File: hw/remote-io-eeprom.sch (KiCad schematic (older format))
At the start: 7 parts, among them P2 CONN_01X02, U3 CAT24C32

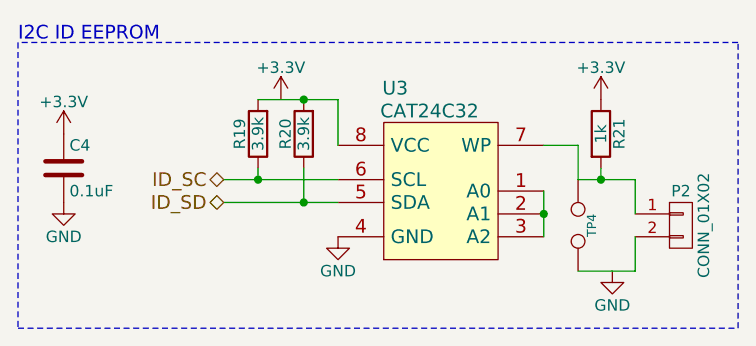
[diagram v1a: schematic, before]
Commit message: Matched all footprints to schem and created kicad_pcb file
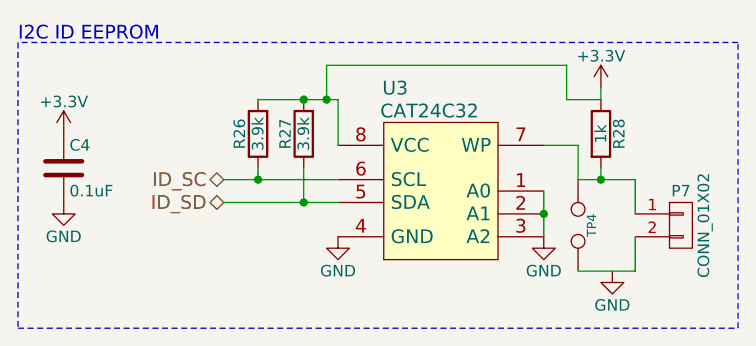
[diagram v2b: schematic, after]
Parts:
- C4: footprint (none) -> Capacitors_SMD:C_0805_HandSoldering
- P7: renamed from P2; footprint (none) -> Pin_Headers:Pin_Header_Straight_1x02
- R26: renamed from R19; footprint (none) -> Resistors_SMD:R_0805_HandSoldering
- R27: renamed from R20; footprint (none) -> Resistors_SMD:R_0805_HandSoldering
- R28: renamed from R21; footprint (none) -> Resistors_SMD:R_0805_HandSoldering
- TP4: footprint (none) -> Connect:TESTPOINT
- U3: footprint (none) -> Housings_SOIC:SOIC-8_3.9x4.9mm_Pitch1.27mm
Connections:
- net +3V3: now also R26.2, R27.2, U3.8 (VCC)
- net GND: now also U3.1 (A0), U3.2 (A1), U3.3 (A2)
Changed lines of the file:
@@
 F 0 "U3" H 4850 3500 60  0000 C CNN
 F 1 "CAT24C32" H 5000 3400 60  0000 C CNN
-F 2 "" H 5200 3050 60  0000 C CNN
+F 2 "Housings_SOIC:SOIC-8_3.9x4.9mm_Pitch1.27mm" H 5200 3050 60  0001 C CNN
 F 3 "" H 5200 3050 60  0000 C CNN
 	1    5050 3100
@@
 F 0 "C4" H 3425 3150 50  0000 L CNN
 F 1 "0.1uF" H 3425 2950 50  0000 L CNN
-F 2 "" H 3438 2900 30  0000 C CNN
+F 2 "Capacitors_SMD:C_0805_HandSoldering" H 3438 2900 30  0001 C CNN
 F 3 "" H 3400 3050 60  0000 C CNN
 	1    3400 3050
@@
 F 0 "TP4" H 5650 3360 40  0000 C CNN
 F 1 "TEST" H 5650 3230 40  0001 C CNN
-F 2 "" H 5650 3300 60  0000 C CNN
+F 2 "Connect:TESTPOINT" H 5650 3300 60  0001 C CNN
 F 3 "" H 5650 3300 60  0000 C CNN
 	1    5650 3300
@@
 $EndComp
 $Comp
-L CONN_01X02 P2
+L CONN_01X02 P7
 U 1 1 558185B6
 P 6100 3300
-F 0 "P2" H 6100 3450 50  0000 C CNN
+F 0 "P7" H 6100 3450 50  0000 C CNN
 F 1 "CONN_01X02" V 6200 3300 50  0000 C CNN
-F 2 "" H 6100 3300 60  0000 C CNN
+F 2 "Pin_Headers:Pin_Header_Straight_1x02" H 6100 3300 60  0001 C CNN
 F 3 "" H 6100 3300 60  0000 C CNN
 	1    6100 3300
@@
 $EndComp
 $Comp
-L R R21
+L R R28
 U 1 1 55818601
 P 5750 2900
-F 0 "R21" V 5830 2900 50  0000 C CNN
+F 0 "R28" V 5830 2900 50  0000 C CNN
 F 1 "1k" V 5750 2900 50  0000 C CNN
-F 2 "" V 5680 2900 30  0000 C CNN
+F 2 "Resistors_SMD:R_0805_HandSoldering" V 5680 2900 30  0001 C CNN
 F 3 "" H 5750 2900 30  0000 C CNN
 	1    5750 2900
@@
 $EndComp
 $Comp
-L R R19
+L R R26
 U 1 1 5581863F
 P 4250 2900
-F 0 "R19" V 4330 2900 50  0000 C CNN
+F 0 "R26" V 4330 2900 50  0000 C CNN
 F 1 "3.9k" V 4250 2900 50  0000 C CNN
-F 2 "" V 4180 2900 30  0000 C CNN
+F 2 "Resistors_SMD:R_0805_HandSoldering" V 4180 2900 30  0001 C CNN
 F 3 "" H 4250 2900 30  0000 C CNN
 	1    4250 2900
@@
 $EndComp
 $Comp
-L R R20
+L R R27
 U 1 1 55818663
 P 4450 2900
-F 0 "R20" V 4530 2900 50  0000 C CNN
+F 0 "R27" V 4530 2900 50  0000 C CNN
 F 1 "3.9k" V 4450 2900 50  0000 C CNN
-F 2 "" V 4380 2900 30  0000 C CNN
+F 2 "Resistors_SMD:R_0805_HandSoldering" V 4380 2900 30  0001 C CNN
 F 3 "" H 4450 2900 30  0000 C CNN
 	1    4450 2900
@@
 $EndComp
 $Comp
-L +3.3V #PWR34
-U 1 1 558186FF
-P 4350 2750
-F 0 "#PWR34" H 4350 2600 50  0001 C CNN
-F 1 "+3.3V" H 4350 2890 50  0000 C CNN
-F 2 "" H 4350 2750 60  0000 C CNN
-F 3 "" H 4350 2750 60  0000 C CNN
-	1    4350 2750
-	1    0    0    -1
-$EndComp
-$Comp
-L +3.3V #PWR36
+L +3.3V #PWR045
 U 1 1 55818752
 P 3400 2900
-F 0 "#PWR36" H 3400 2750 50  0001 C CNN
+F 0 "#PWR045" H 3400 2750 50  0001 C CNN
 F 1 "+3.3V" H 3400 3040 50  0000 C CNN
 F 2 "" H 3400 2900 60  0000 C CNN
@@
 $EndComp
 $Comp
-L GND #PWR37
-U 1 1 55818774
-P 3400 3200
-F 0 "#PWR37" H 3400 2950 50  0001 C CNN
-F 1 "GND" H 3400 3050 50  0000 C CNN
-F 2 "" H 3400 3200 60  0000 C CNN
-F 3 "" H 3400 3200 60  0000 C CNN
-	1    3400 3200
-	1    0    0    -1
-$EndComp
-$Comp
-L GND #PWR38
-U 1 1 55818794
-P 4600 3350
-F 0 "#PWR38" H 4600 3100 50  0001 C CNN
-F 1 "GND" H 4600 3200 50  0000 C CNN
-F 2 "" H 4600 3350 60  0000 C CNN
-F 3 "" H 4600 3350 60  0000 C CNN
-	1    4600 3350
-	1    0    0    -1
-$EndComp
-$Comp
-L GND #PWR39
-U 1 1 55818DF1
-P 5800 3500
-F 0 "#PWR39" H 5800 3250 50  0001 C CNN
-F 1 "GND" H 5800 3350 50  0000 C CNN
-F 2 "" H 5800 3500 60  0000 C CNN
-F 3 "" H 5800 3500 60  0000 C CNN
-	1    5800 3500
-	1    0    0    -1
-$EndComp
-$Comp
-L +3.3V #PWR35
+L +3.3V #PWR046
 U 1 1 558190BD
-P 5750 2750
-F 0 "#PWR35" H 5750 2600 50  0001 C CNN
-F 1 "+3.3V" H 5750 2890 50  0000 C CNN
-F 2 "" H 5750 2750 60  0000 C CNN
-F 3 "" H 5750 2750 60  0000 C CNN
-	1    5750 2750
+P 5750 2700
+F 0 "#PWR046" H 5750 2550 50  0001 C CNN
+F 1 "+3.3V" H 5750 2840 50  0000 C CNN
+F 2 "" H 5750 2700 60  0000 C CNN
+F 3 "" H 5750 2700 60  0000 C CNN
+	1    5750 2700
 	1    0    0    -1
 $EndComp
@@
 Wire Wire Line
 	4250 2750 4600 2750
-Wire Wire Line
-	4600 2750 4600 2950
 Connection ~ 4450 2750
 Wire Wire Line
@@
 Text Notes 3200 2500 0    60   ~ 0
 I2C ID EEPROM
+Wire Wire Line
+	4600 2750 4600 2950
+Wire Wire Line
+	4550 2750 4550 2600
+Wire Wire Line
+	4550 2600 5600 2600
+Wire Wire Line
+	5600 2600 5600 2750
+Wire Wire Line
+	5600 2750 5750 2750
+Connection ~ 4550 2750
+Wire Wire Line
+	5750 2750 5750 2700
+$Comp
+L GND #PWR047
+U 1 1 55818DF1
+P 5800 3500
+F 0 "#PWR047" H 5800 3250 50  0001 C CNN
+F 1 "GND" H 5800 3350 50  0000 C CNN
+F 2 "" H 5800 3500 60  0000 C CNN
+F 3 "" H 5800 3500 60  0000 C CNN
+	1    5800 3500
+	1    0    0    -1
+$EndComp
+$Comp
+L GND #PWR048
+U 1 1 5581AAA1
+P 5500 3350
+F 0 "#PWR048" H 5500 3100 50  0001 C CNN
+F 1 "GND" H 5500 3200 50  0000 C CNN
+F 2 "" H 5500 3350 60  0000 C CNN
+F 3 "" H 5500 3350 60  0000 C CNN
+	1    5500 3350
+	1    0    0    -1
+$EndComp
+$Comp
+L GND #PWR049
+U 1 1 55818794
+P 4600 3350
+F 0 "#PWR049" H 4600 3100 50  0001 C CNN
+F 1 "GND" H 4600 3200 50  0000 C CNN
+F 2 "" H 4600 3350 60  0000 C CNN
+F 3 "" H 4600 3350 60  0000 C CNN
+	1    4600 3350
+	1    0    0    -1
+$EndComp
+$Comp
+L GND #PWR050
+U 1 1 55818774
+P 3400 3200
+F 0 "#PWR050" H 3400 2950 50  0001 C CNN
+F 1 "GND" H 3400 3050 50  0000 C CNN
+F 2 "" H 3400 3200 60  0000 C CNN
+F 3 "" H 3400 3200 60  0000 C CNN
+	1    3400 3200
+	1    0    0    -1
+$EndComp
 $EndSCHEMATC

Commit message: removed autosave
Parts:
- TP4: footprint Connect:TESTPOINT -> Pin_Headers:Pin_Header_Straight_1x02
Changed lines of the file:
@@
 F 0 "TP4" H 5650 3360 40  0000 C CNN
 F 1 "TEST" H 5650 3230 40  0001 C CNN
-F 2 "Connect:TESTPOINT" H 5650 3300 60  0001 C CNN
+F 2 "Pin_Headers:Pin_Header_Straight_1x02" H 5650 3300 60  0001 C CNN
 F 3 "" H 5650 3300 60  0000 C CNN
 	1    5650 3300

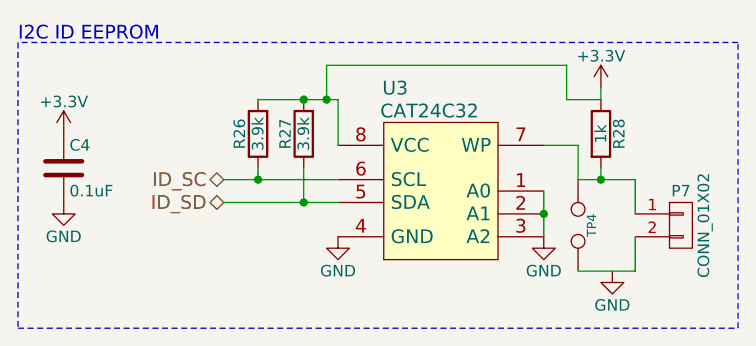
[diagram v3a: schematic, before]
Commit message: added CAN power, controller, and transceiver to schem and updated PCB
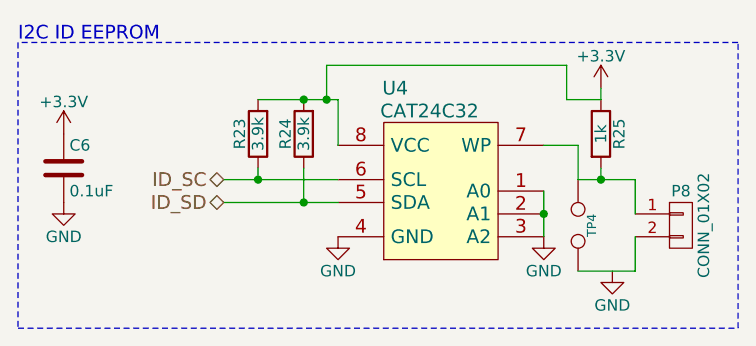
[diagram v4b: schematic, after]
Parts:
- renumbered C4 to C6, P7 to P8, R26 to R23, R27 to R24, R28 to R25, U3 to U4
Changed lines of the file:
@@
 $Descr USLetter 11000 8500
 encoding utf-8
-Sheet 4 5
+Sheet 4 6
 Title "I2C ID EEPROM"
 Date "2015-06-15"
@@
 $EndDescr
 $Comp
-L CAT24C32 U3
+L CAT24C32 U4
 U 1 1 558183DB
 P 5050 3100
-F 0 "U3" H 4850 3500 60  0000 C CNN
+F 0 "U4" H 4850 3500 60  0000 C CNN
 F 1 "CAT24C32" H 5000 3400 60  0000 C CNN
 F 2 "Housings_SOIC:SOIC-8_3.9x4.9mm_Pitch1.27mm" H 5200 3050 60  0001 C CNN
@@
 $EndComp
 $Comp
-L C C4
+L C C6
 U 1 1 5581842A
 P 3400 3050
-F 0 "C4" H 3425 3150 50  0000 L CNN
+F 0 "C6" H 3425 3150 50  0000 L CNN
 F 1 "0.1uF" H 3425 2950 50  0000 L CNN
 F 2 "Capacitors_SMD:C_0805_HandSoldering" H 3438 2900 30  0001 C CNN
@@
 $EndComp
 $Comp
-L CONN_01X02 P7
+L CONN_01X02 P8
 U 1 1 558185B6
 P 6100 3300
-F 0 "P7" H 6100 3450 50  0000 C CNN
+F 0 "P8" H 6100 3450 50  0000 C CNN
 F 1 "CONN_01X02" V 6200 3300 50  0000 C CNN
 F 2 "Pin_Headers:Pin_Header_Straight_1x02" H 6100 3300 60  0001 C CNN
@@
 $EndComp
 $Comp
-L R R28
+L R R25
 U 1 1 55818601
 P 5750 2900
-F 0 "R28" V 5830 2900 50  0000 C CNN
+F 0 "R25" V 5830 2900 50  0000 C CNN
 F 1 "1k" V 5750 2900 50  0000 C CNN
 F 2 "Resistors_SMD:R_0805_HandSoldering" V 5680 2900 30  0001 C CNN
@@
 $EndComp
 $Comp
-L R R26
+L R R23
 U 1 1 5581863F
 P 4250 2900
-F 0 "R26" V 4330 2900 50  0000 C CNN
+F 0 "R23" V 4330 2900 50  0000 C CNN
 F 1 "3.9k" V 4250 2900 50  0000 C CNN
 F 2 "Resistors_SMD:R_0805_HandSoldering" V 4180 2900 30  0001 C CNN
@@
 $EndComp
 $Comp
-L R R27
+L R R24
 U 1 1 55818663
 P 4450 2900
-F 0 "R27" V 4530 2900 50  0000 C CNN
+F 0 "R24" V 4530 2900 50  0000 C CNN
 F 1 "3.9k" V 4450 2900 50  0000 C CNN
 F 2 "Resistors_SMD:R_0805_HandSoldering" V 4380 2900 30  0001 C CNN
@@
 $EndComp
 $Comp
-L +3.3V #PWR045
+L +3.3V #PWR051
 U 1 1 55818752
 P 3400 2900
-F 0 "#PWR045" H 3400 2750 50  0001 C CNN
+F 0 "#PWR051" H 3400 2750 50  0001 C CNN
 F 1 "+3.3V" H 3400 3040 50  0000 C CNN
 F 2 "" H 3400 2900 60  0000 C CNN
@@
 $EndComp
 $Comp
-L +3.3V #PWR046
+L +3.3V #PWR052
 U 1 1 558190BD
 P 5750 2700
-F 0 "#PWR046" H 5750 2550 50  0001 C CNN
+F 0 "#PWR052" H 5750 2550 50  0001 C CNN
 F 1 "+3.3V" H 5750 2840 50  0000 C CNN
 F 2 "" H 5750 2700 60  0000 C CNN
@@
 	5750 2750 5750 2700
 $Comp
-L GND #PWR047
+L GND #PWR053
 U 1 1 55818DF1
 P 5800 3500
-F 0 "#PWR047" H 5800 3250 50  0001 C CNN
+F 0 "#PWR053" H 5800 3250 50  0001 C CNN
 F 1 "GND" H 5800 3350 50  0000 C CNN
 F 2 "" H 5800 3500 60  0000 C CNN
@@
 $EndComp
 $Comp
-L GND #PWR048
+L GND #PWR054
 U 1 1 5581AAA1
 P 5500 3350
-F 0 "#PWR048" H 5500 3100 50  0001 C CNN
+F 0 "#PWR054" H 5500 3100 50  0001 C CNN
 F 1 "GND" H 5500 3200 50  0000 C CNN
 F 2 "" H 5500 3350 60  0000 C CNN
@@
 $EndComp
 $Comp
-L GND #PWR049
+L GND #PWR055
 U 1 1 55818794
 P 4600 3350
-F 0 "#PWR049" H 4600 3100 50  0001 C CNN
+F 0 "#PWR055" H 4600 3100 50  0001 C CNN
 F 1 "GND" H 4600 3200 50  0000 C CNN
 F 2 "" H 4600 3350 60  0000 C CNN
@@
 $EndComp
 $Comp
-L GND #PWR050
+L GND #PWR056
 U 1 1 55818774
 P 3400 3200
-F 0 "#PWR050" H 3400 2950 50  0001 C CNN
+F 0 "#PWR056" H 3400 2950 50  0001 C CNN
 F 1 "GND" H 3400 3050 50  0000 C CNN
 F 2 "" H 3400 3200 60  0000 C CNN

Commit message: Started fucking aroond with pcb layout. Power is tricky...
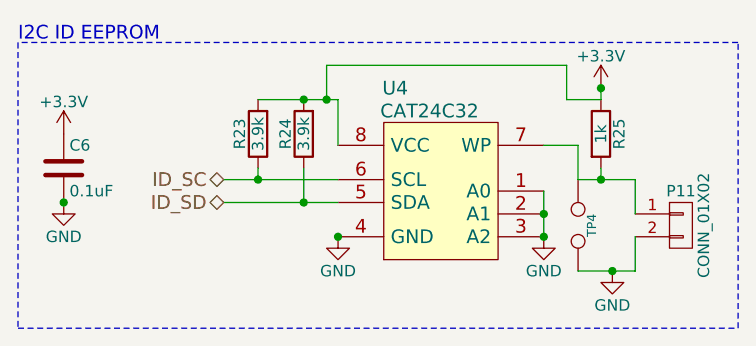
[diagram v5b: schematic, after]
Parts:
- renumbered P8 to P11
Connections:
- net GND: now also P11.2 (P2), TP4.2
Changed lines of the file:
@@
 $EndComp
 $Comp
-L CONN_01X02 P8
+L CONN_01X02 P11
 U 1 1 558185B6
 P 6100 3300
-F 0 "P8" H 6100 3450 50  0000 C CNN
+F 0 "P11" H 6100 3450 50  0000 C CNN
 F 1 "CONN_01X02" V 6200 3300 50  0000 C CNN
 F 2 "Pin_Headers:Pin_Header_Straight_1x02" H 6100 3300 60  0001 C CNN
@@
 $EndComp
 $Comp
-L +3.3V #PWR051
+L +3.3V #PWR048
 U 1 1 55818752
 P 3400 2900
-F 0 "#PWR051" H 3400 2750 50  0001 C CNN
+F 0 "#PWR048" H 3400 2750 50  0001 C CNN
 F 1 "+3.3V" H 3400 3040 50  0000 C CNN
 F 2 "" H 3400 2900 60  0000 C CNN
@@
 $EndComp
 $Comp
-L +3.3V #PWR052
+L +3.3V #PWR049
 U 1 1 558190BD
 P 5750 2700
-F 0 "#PWR052" H 5750 2550 50  0001 C CNN
+F 0 "#PWR049" H 5750 2550 50  0001 C CNN
 F 1 "+3.3V" H 5750 2840 50  0000 C CNN
 F 2 "" H 5750 2700 60  0000 C CNN
@@
 	5750 2750 5750 2700
 $Comp
-L GND #PWR053
+L GND #PWR050
 U 1 1 55818DF1
 P 5800 3500
-F 0 "#PWR053" H 5800 3250 50  0001 C CNN
+F 0 "#PWR050" H 5800 3250 50  0001 C CNN
 F 1 "GND" H 5800 3350 50  0000 C CNN
 F 2 "" H 5800 3500 60  0000 C CNN
@@
 $EndComp
 $Comp
-L GND #PWR054
+L GND #PWR051
 U 1 1 5581AAA1
 P 5500 3350
-F 0 "#PWR054" H 5500 3100 50  0001 C CNN
+F 0 "#PWR051" H 5500 3100 50  0001 C CNN
 F 1 "GND" H 5500 3200 50  0000 C CNN
 F 2 "" H 5500 3350 60  0000 C CNN
@@
 $EndComp
 $Comp
-L GND #PWR055
+L GND #PWR052
 U 1 1 55818794
 P 4600 3350
-F 0 "#PWR055" H 4600 3100 50  0001 C CNN
+F 0 "#PWR052" H 4600 3100 50  0001 C CNN
 F 1 "GND" H 4600 3200 50  0000 C CNN
 F 2 "" H 4600 3350 60  0000 C CNN
@@
 $EndComp
 $Comp
-L GND #PWR056
+L GND #PWR053
 U 1 1 55818774
 P 3400 3200
-F 0 "#PWR056" H 3400 2950 50  0001 C CNN
+F 0 "#PWR053" H 3400 2950 50  0001 C CNN
 F 1 "GND" H 3400 3050 50  0000 C CNN
 F 2 "" H 3400 3200 60  0000 C CNN
@@
 	1    0    0    -1
 $EndComp
+Connection ~ 5500 3350
+Connection ~ 5800 3500
+Connection ~ 4600 3350
+Connection ~ 3400 3200
+Connection ~ 5750 2700
 $EndSCHEMATC
